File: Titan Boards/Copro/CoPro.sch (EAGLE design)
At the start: 82 parts, among them P2 RB1-125BAG1A, Q1 310mA/60V/1.6Ω, Q10 310mA/60V/1.6Ω, Q2 310mA/60V/1.6Ω, Q3 310mA/60V/1.6Ω, Q4 310mA/60V/1.6Ω, Q5 310mA/60V/1.6Ω, Q6 310mA/60V/1.6Ω, Q7 310mA/60V/1.6Ω, Q8 310mA/60V/1.6Ω, Q9 310mA/60V/1.6Ω, U1 SN74LVC3G04DCUT, U2 SN74LVC1G11DCKR, Y1 25Mhz, Y2 12MHz, Y3 32.768kHz

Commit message: Copro Board Work
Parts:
- removed 165, 250: (no value), rcl:R-US_0204/7
- added R43: 165, rcl:R-US_R0603
- added R44: 250, rcl:R-US_R0603
- R13, R14: device rcl:R-US_0204/7 -> rcl:R-US_R0603
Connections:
- removed net PWN_3V3_1: Q9.S, R1.2
- new net PWM_3V3_1: Q9.S, R1.2, STM32.PA0/WKUP
- net LED_3V3: now also R43.1; no longer 165.1
- net LED_5V: now also R44.1; no longer 250.1
- net N$34: now also R43.2; no longer 165.2
- net N$37: now also R44.2; no longer 250.2
- net PWM_1: no longer STM32.PA0/WKUP
- net PWM_10: no longer STM32.PB9
- net PWM_2: no longer STM32.PA1/USART2_RTS
- net PWM_3: no longer STM32.PA2/USART2_TX
- net PWM_3V3_10: now also STM32.PB9
- net PWM_3V3_2: now also STM32.PA1/USART2_RTS
- net PWM_3V3_3: now also STM32.PA2/USART2_TX
- net PWM_3V3_4: now also STM32.PA3/USART2_RX
- net PWM_3V3_5: now also STM32.PC6
- net PWM_3V3_6: now also STM32.PC7
- net PWM_3V3_7: now also STM32.PC8
- net PWM_3V3_8: now also STM32.PC9
- net PWM_3V3_9: now also STM32.PB8
- net PWM_4: no longer STM32.PA3/USART2_RX
- net PWM_5: no longer STM32.PC6
- net PWM_6: no longer STM32.PC7
- net PWM_7: no longer STM32.PC8
- net PWM_8: no longer STM32.PC9
- net PWM_9: no longer STM32.PB8

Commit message: Finished Copro V1
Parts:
- added R17: 0, rcl:R-US_R0603
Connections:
- net ROBOT_SDA: now also R17.1, R17.2
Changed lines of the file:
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@@
 <part name="GND12" library="supply1" library_urn="urn:adsk.eagle:library:371" deviceset="GND" device=""/>
 <part name="FRAME4" library="frames" library_urn="urn:adsk.eagle:library:229" deviceset="A3L-LOC" device="" value="a"/>
+<part name="R17" library="rcl" library_urn="urn:adsk.eagle:library:334" deviceset="R-US_" device="R0603" package3d_urn="urn:adsk.eagle:package:23555/3" value="0"/>
 </parts>
 <sheets>
@@
 <attribute name="VALUE" x="134.62" y="223.52" size="1.778" layer="96" rot="R90"/>
 </instance>
+<instance part="R17" gate="G$1" x="215.9" y="134.62" smashed="yes">
+<attribute name="NAME" x="212.09" y="136.1186" size="1.778" layer="95"/>
+<attribute name="VALUE" x="212.09" y="131.318" size="1.778" layer="96"/>
+</instance>
 </instances>
 <busses>
@@
 <pinref part="STM32" gate="G$1" pin="PB11"/>
 <wire x1="248.92" y1="134.62" x2="220.98" y2="134.62" width="0.1524" layer="91"/>
-<label x="220.98" y="134.62" size="1.778" layer="95" rot="R180" xref="yes"/>
+<pinref part="R17" gate="G$1" pin="2"/>
+</segment>
+<segment>
+<wire x1="210.82" y1="134.62" x2="203.2" y2="134.62" width="0.1524" layer="91"/>
+<label x="203.2" y="134.62" size="1.778" layer="95" rot="R180" xref="yes"/>
+<pinref part="R17" gate="G$1" pin="1"/>
 </segment>
 </net>

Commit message: Schem Updates
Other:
- note added: "Additional Standard Components: -LED's -Resistors -Capacitors -Diodes -Switch"
- note added: "Administrative Notes: Board Name: Titan CoPro Schematic Creation: 09/2020 Schematic Designers: David Chen, Nathan Ayer Electrical Lead: Phillip Barker"
- note added: "Datasheet: https://assets.nexperia.com/documents/data-sheet/2N7002PW.pdf"
- note added: "HC49US Digikey: https://www.digikey.com/catalog/en/partgroup/hc-49us-series/4765"
- note added: "MHz Crystals:"
- note added: "Mosfets: MOSFET-NCH-2N7002PW"
- note added: "SMD 32.768 kHz Newark : https://www.newark.com/c/crystals-oscillators/crystals? brand=abracon&crystal-case=smd-3.2mm-x-1.5mm"
- note added: "https://www.nexperia.com/products/mosfets/small-signal-mosfets/2N7002PW.html"
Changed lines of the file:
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@@
 <?xml version="1.0" encoding="utf-8"?>
 <!DOCTYPE eagle SYSTEM "eagle.dtd">
-<eagle version="9.6.2">
+<eagle version="9.5.0">
 <drawing>
 <settings>
@@
 <text x="17.78" y="152.4" size="3.81" layer="91">https://www.snapeda.com/parts/SN74LVC1G11DCKR/Texas%20Instruments
 /view-part/?ref=search&amp;t=SN74LVC1G11</text>
+<text x="289.56" y="200.66" size="4.064" layer="91">Additional Standard Components:
+-LED's
+-Resistors
+-Capacitors
+-Diodes
+-Switch</text>
+<text x="289.56" y="154.94" size="4.064" layer="91">Administrative Notes:
+Board Name: Titan CoPro
+Schematic Creation: 09/2020
+Schematic Designers:
+David Chen, Nathan Ayer
+Electrical Lead: Phillip Barker</text>
+<text x="17.78" y="142.24" size="4.064" layer="91">MHz Crystals:</text>
+<text x="17.78" y="137.16" size="4.064" layer="91">HC49US Digikey: https://www.digikey.com/catalog/en/partgroup/hc-49us-series/4765</text>
+<text x="17.78" y="124.46" size="4.064" layer="91">SMD 32.768 kHz Newark : https://www.newark.com/c/crystals-oscillators/crystals?
+brand=abracon&amp;crystal-case=smd-3.2mm-x-1.5mm</text>
+<text x="17.78" y="114.3" size="4.064" layer="91">Mosfets: MOSFET-NCH-2N7002PW</text>
+<text x="17.78" y="109.22" size="4.064" layer="91">Datasheet: https://assets.nexperia.com/documents/data-sheet/2N7002PW.pdf</text>
+<text x="17.78" y="104.14" size="4.064" layer="91">https://www.nexperia.com/products/mosfets/small-signal-mosfets/2N7002PW.html</text>
 </plain>
 <instances>

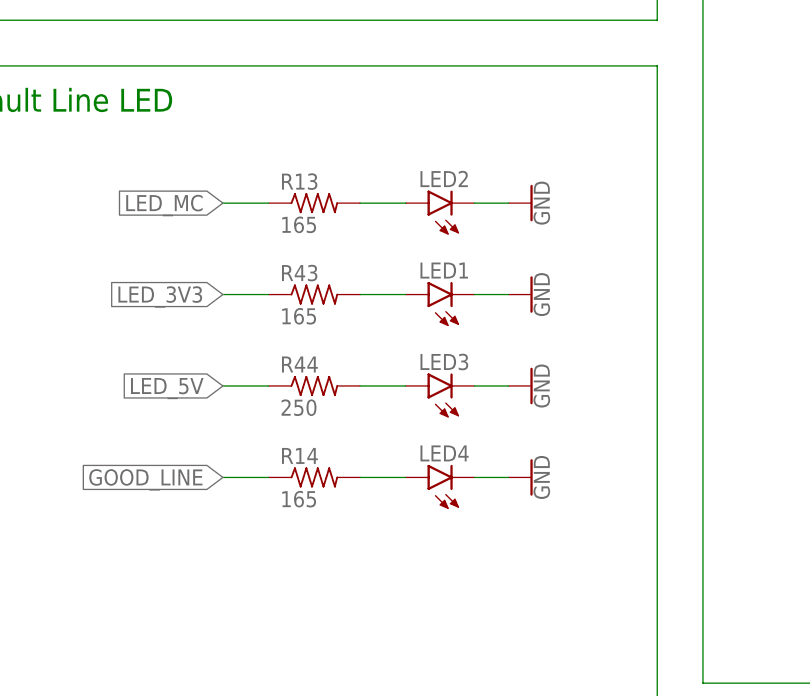
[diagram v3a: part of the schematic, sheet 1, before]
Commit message: light board review changes
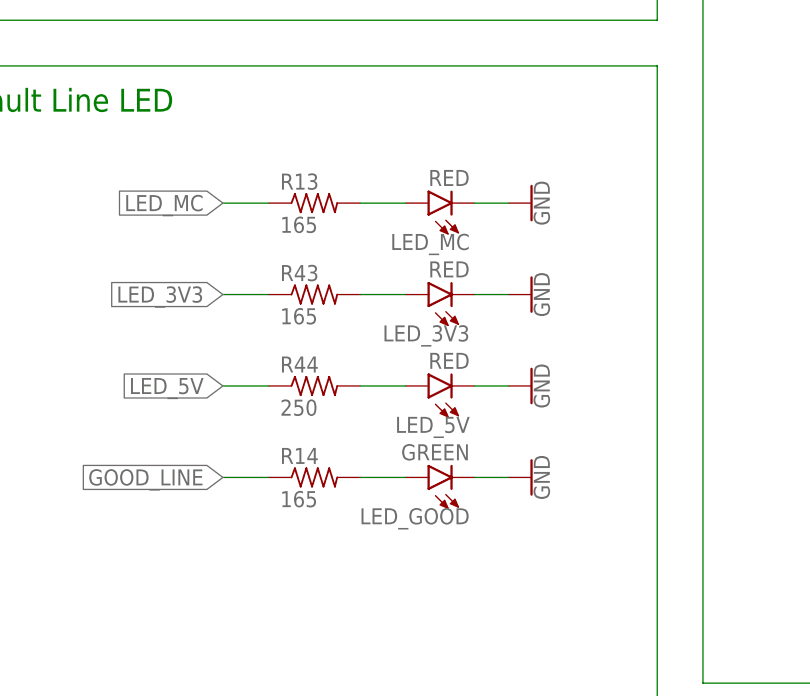
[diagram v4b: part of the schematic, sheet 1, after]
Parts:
- removed LED1, LED2, LED3, LED4: (no value), led:LED
- added LED_3V3, LED_5V, LED_MC: RED, SparkFun-LED:LED0603
- added LED_GOOD: GREEN, SparkFun-LED:LED0603
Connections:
- net GND: now also LED_3V3.C, LED_5V.C, LED_GOOD.C, LED_MC.C; no longer LED1.C, LED2.C, LED3.C, LED4.C
- net N$34: now also LED_3V3.A; no longer LED1.A
- net N$37: now also LED_5V.A; no longer LED3.A
- net N$38: now also LED_GOOD.A; no longer LED4.A
- net N$8: now also LED_MC.A; no longer LED2.A
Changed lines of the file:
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@@
 <?xml version="1.0" encoding="utf-8"?>
 <!DOCTYPE eagle SYSTEM "eagle.dtd">
-<eagle version="9.5.0">
+<eagle version="9.5.1">
 <drawing>
 <settings>
@@
 <part name="D1" library="diode" library_urn="urn:adsk.eagle:library:210" deviceset="DIODE-" device="SMB" package3d_urn="urn:adsk.eagle:package:43404/2"/>
 <part name="GND6" library="SparkFun-PowerSymbols" library_urn="urn:adsk.eagle:library:530" deviceset="GND" device=""/>
-<part name="LED2" library="led" library_urn="urn:adsk.eagle:library:259" deviceset="LED" device="" package3d_urn="urn:adsk.eagle:package:15825/1"/>
-<part name="LED1" library="led" library_urn="urn:adsk.eagle:library:259" deviceset="LED" device="" package3d_urn="urn:adsk.eagle:package:15825/1"/>
-<part name="LED3" library="led" library_urn="urn:adsk.eagle:library:259" deviceset="LED" device="" package3d_urn="urn:adsk.eagle:package:15825/1"/>
 <part name="GND2" library="SparkFun-PowerSymbols" library_urn="urn:adsk.eagle:library:530" deviceset="GND" device=""/>
 <part name="GND7" library="SparkFun-PowerSymbols" library_urn="urn:adsk.eagle:library:530" deviceset="GND" device=""/>
@@
 <part name="R43" library="rcl" library_urn="urn:adsk.eagle:library:334" deviceset="R-US_" device="R0603" package3d_urn="urn:adsk.eagle:package:23555/3" value="165"/>
 <part name="R44" library="rcl" library_urn="urn:adsk.eagle:library:334" deviceset="R-US_" device="R0603" package3d_urn="urn:adsk.eagle:package:23555/3" value="250"/>
-<part name="LED4" library="led" library_urn="urn:adsk.eagle:library:259" deviceset="LED" device="" package3d_urn="urn:adsk.eagle:package:15825/1"/>
 <part name="GND9" library="SparkFun-PowerSymbols" library_urn="urn:adsk.eagle:library:530" deviceset="GND" device=""/>
 <part name="R14" library="rcl" library_urn="urn:adsk.eagle:library:334" deviceset="R-US_" device="R0603" package3d_urn="urn:adsk.eagle:package:23555/3" value="165"/>
@@
 <part name="FRAME4" library="frames" library_urn="urn:adsk.eagle:library:229" deviceset="A3L-LOC" device="" value="a"/>
 <part name="R17" library="rcl" library_urn="urn:adsk.eagle:library:334" deviceset="R-US_" device="R0603" package3d_urn="urn:adsk.eagle:package:23555/3" value="0"/>
+<part name="LED_MC" library="SparkFun-LED" library_urn="urn:adsk.eagle:library:529" deviceset="LED" device="0603" package3d_urn="urn:adsk.eagle:package:39354/1" value="RED"/>
+<part name="LED_3V3" library="SparkFun-LED" library_urn="urn:adsk.eagle:library:529" deviceset="LED" device="0603" package3d_urn="urn:adsk.eagle:package:39354/1" value="RED"/>
+<part name="LED_5V" library="SparkFun-LED" library_urn="urn:adsk.eagle:library:529" deviceset="LED" device="0603" package3d_urn="urn:adsk.eagle:package:39354/1" value="RED"/>
+<part name="LED_GOOD" library="SparkFun-LED" library_urn="urn:adsk.eagle:library:529" deviceset="LED" device="0603" package3d_urn="urn:adsk.eagle:package:39354/1" value="GREEN"/>
 </parts>
 <sheets>
@@
 <attribute name="VALUE" x="54.61" y="119.126" size="1.778" layer="96" align="top-center"/>
 </instance>
-<instance part="LED2" gate="G$1" x="63.5" y="83.82" smashed="yes" rot="R90">
-<attribute name="NAME" x="68.072" y="87.376" size="1.778" layer="95" rot="R180"/>
-<attribute name="VALUE" x="68.072" y="89.535" size="1.778" layer="96" rot="R180"/>
-</instance>
-<instance part="LED1" gate="G$1" x="63.5" y="73.66" smashed="yes" rot="R90">
-<attribute name="NAME" x="68.072" y="77.216" size="1.778" layer="95" rot="R180"/>
-<attribute name="VALUE" x="68.072" y="79.375" size="1.778" layer="96" rot="R180"/>
-</instance>
-<instance part="LED3" gate="G$1" x="63.5" y="63.5" smashed="yes" rot="R90">
-<attribute name="NAME" x="68.072" y="67.056" size="1.778" layer="95" rot="R180"/>
-<attribute name="VALUE" x="68.072" y="69.215" size="1.778" layer="96" rot="R180"/>
-</instance>
 <instance part="GND2" gate="1" x="74.93" y="83.82" smashed="yes" rot="R90">
 <attribute name="VALUE" x="75.184" y="83.82" size="1.778" layer="96" rot="R90" align="top-center"/>
@@
 <attribute name="VALUE" x="46.99" y="60.198" size="1.778" layer="96"/>
 </instance>
-<instance part="LED4" gate="G$1" x="63.5" y="53.34" smashed="yes" rot="R90">
-<attribute name="NAME" x="68.072" y="56.896" size="1.778" layer="95" rot="R180"/>
-<attribute name="VALUE" x="68.072" y="59.055" size="1.778" layer="96" rot="R180"/>
-</instance>
 <instance part="GND9" gate="1" x="74.93" y="53.34" smashed="yes" rot="R90">
 <attribute name="VALUE" x="75.184" y="53.34" size="1.778" layer="96" rot="R90" align="top-center"/>
@@
 <attribute name="VALUE" x="46.99" y="50.038" size="1.778" layer="96"/>
 </instance>
+<instance part="LED_MC" gate="G$1" x="63.5" y="83.82" smashed="yes" rot="R90">
+<attribute name="NAME" x="68.072" y="80.391" size="1.778" layer="95" font="vector" rot="R180"/>
+<attribute name="VALUE" x="68.072" y="85.725" size="1.778" layer="96" font="vector" rot="R180" align="top-left"/>
+</instance>
+<instance part="LED_3V3" gate="G$1" x="63.5" y="73.66" smashed="yes" rot="R90">
+<attribute name="NAME" x="68.072" y="70.231" size="1.778" layer="95" font="vector" rot="R180"/>
+<attribute name="VALUE" x="68.072" y="75.565" size="1.778" layer="96" font="vector" rot="R180" align="top-left"/>
+</instance>
+<instance part="LED_5V" gate="G$1" x="63.5" y="63.5" smashed="yes" rot="R90">
+<attribute name="NAME" x="68.072" y="60.071" size="1.778" layer="95" font="vector" rot="R180"/>
+<attribute name="VALUE" x="68.072" y="65.405" size="1.778" layer="96" font="vector" rot="R180" align="top-left"/>
+</instance>
+<instance part="LED_GOOD" gate="G$1" x="63.5" y="53.34" smashed="yes" rot="R90">
+<attribute name="NAME" x="68.072" y="49.911" size="1.778" layer="95" font="vector" rot="R180"/>
+<attribute name="VALUE" x="68.072" y="55.245" size="1.778" layer="96" font="vector" rot="R180" align="top-left"/>
+</instance>
 </instances>
 <busses>
@@
 </segment>
 <segment>
-<pinref part="LED2" gate="G$1" pin="C"/>
 <pinref part="GND2" gate="1" pin="GND"/>
 <wire x1="68.58" y1="83.82" x2="72.39" y2="83.82" width="0.1524" layer="91"/>
+<pinref part="LED_MC" gate="G$1" pin="C"/>
 </segment>
 <segment>
-<pinref part="LED1" gate="G$1" pin="C"/>
 <pinref part="GND7" gate="1" pin="GND"/>
 <wire x1="68.58" y1="73.66" x2="72.39" y2="73.66" width="0.1524" layer="91"/>
+<pinref part="LED_3V3" gate="G$1" pin="C"/>
 </segment>
 <segment>
-<pinref part="LED3" gate="G$1" pin="C"/>
 <pinref part="GND8" gate="1" pin="GND"/>
 <wire x1="68.58" y1="63.5" x2="72.39" y2="63.5" width="0.1524" layer="91"/>
+<pinref part="LED_5V" gate="G$1" pin="C"/>
 </segment>
 <segment>
-<pinref part="LED4" gate="G$1" pin="C"/>
 <pinref part="GND9" gate="1" pin="GND"/>
 <wire x1="68.58" y1="53.34" x2="72.39" y2="53.34" width="0.1524" layer="91"/>
+<pinref part="LED_GOOD" gate="G$1" pin="C"/>
 </segment>
 </net>
@@
 <net name="N$8" class="0">
 <segment>
-<pinref part="LED2" gate="G$1" pin="A"/>
 <wire x1="60.96" y1="83.82" x2="55.88" y2="83.82" width="0.1524" layer="91"/>
 <pinref part="R13" gate="G$1" pin="2"/>
+<pinref part="LED_MC" gate="G$1" pin="A"/>
 </segment>
 </net>
 <net name="N$34" class="0">
 <segment>
-<pinref part="LED1" gate="G$1" pin="A"/>
 <wire x1="60.96" y1="73.66" x2="55.88" y2="73.66" width="0.1524" layer="91"/>
 <pinref part="R43" gate="G$1" pin="2"/>
+<pinref part="LED_3V3" gate="G$1" pin="A"/>
 </segment>
 </net>
 <net name="N$37" class="0">
 <segment>
-<pinref part="LED3" gate="G$1" pin="A"/>
 <wire x1="60.96" y1="63.5" x2="55.88" y2="63.5" width="0.1524" layer="91"/>
 <pinref part="R44" gate="G$1" pin="2"/>
+<pinref part="LED_5V" gate="G$1" pin="A"/>
 </segment>
 </net>
@@
 <net name="N$38" class="0">
 <segment>
-<pinref part="LED4" gate="G$1" pin="A"/>
 <wire x1="60.96" y1="53.34" x2="55.88" y2="53.34" width="0.1524" layer="91"/>
 <pinref part="R14" gate="G$1" pin="2"/>
+<pinref part="LED_GOOD" gate="G$1" pin="A"/>
 </segment>
 </net>

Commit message: Board Review schem changes pt 1.
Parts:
- removed C24: 0.1uF, rcl:C-EUC0603
- removed D1: (no value), diode:DIODE-SMB
- removed R11: 10k, rcl:R-US_R0603
- removed R12: 33k, rcl:R-US_R0603
- removed R17: 0, rcl:R-US_R0603
- added C1, C2, C3, C4, C5: 0.1uF, rcl:C-EUC0603
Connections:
- removed net VBUS1: D1.A, PROGRAMMING1.VBUS
- removed net VBUS_3.3: R11.2, R12.1
- new net MOBO_ON/OFF: STM32.PC2/SPI2_MISO, U$1.MOBO_ON/OFF
- net +3V3: now also C1.1, C2.1, C3.1, C4.1, C5.1; no longer C23.1, C24.1
- net GND: now also C1.2, C2.2, C23.1, C3.2, C4.2, C5.2; no longer R12.2
- net N$36: now also C23.2, R27.1, RESET.2, STM32.NRST; no longer D1.C, R11.1
- net RESET: no longer C23.2, C24.2, R27.1, RESET.2, STM32.NRST
- net ROBOT_SDA: no longer R17.1, R17.2
- net SPARE_5: now also STM32.PB15; no longer STM32.PC2/SPI2_MISO
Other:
- note added: "Connect these to 3V3 on ethernet MC"
- note added: "Decoupling capacitors"
- note added: "needs 5 decoupling capacitors added total."
- note removed: "Added diode recalculated voltage divider was 5k/10k"
- moved on the sheet: C23, LED_3V3, LED_5V, LED_GOOD, LED_MC, PROGRAMMING1, R13, R14, R27, R43, R44, RESET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
